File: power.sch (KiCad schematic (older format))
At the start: 33 parts, among them U3 M3406, U4 XC6206P25, U5 XC6206P12, U6 ME2108A33M3, U7 ME2108A50M3

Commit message: Proto 1
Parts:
- added SW9: SW_SPDT_shielded, lib:Korean_Hroparts_K3_1296S, symbol spdt_sh:SW_SPDT_shielded
- L1: value 2u2 -> SWPA252010S4R7MT; footprint Inductor_SMD:L_1206_3216Metric_Pad1.42x1.75mm_HandSolder -> lib:SWPA25xx
- L2: renamed from L3; value 47u -> SWPA6045S470MT; footprint Inductor_SMD:L_1206_3216Metric_Pad1.42x1.75mm_HandSolder -> lib:SWPA60xx
- L3: renamed from L2; value 47u -> SWPA6045S470MT; footprint Inductor_SMD:L_1206_3216Metric_Pad1.42x1.75mm_HandSolder -> lib:SWPA60xx
- renumbered C27 to C21, C1 to C22, C28 to C23, C29 to C24, C30 to C25, C48 to C26, C49 to C27, C50 to C28, C31 to C29, C32 to C30, C33 to C31, C34 to C32, C35 to C33, D4 to D1, D1 to D2, R28 to R17, R11 to R18, R12 to R19, R29 to R20, R32 to R21, R13 to R22, R30 to R23, R31 to R24, U3 to U5, U4 to U6, U5 to U8, U6 to U9
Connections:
- net labels added: VBAT_ALWON
- wire segments 70 -> 72
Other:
- note added: "L2: 1-4.7uH, 50-150mR\n(is 4.7uH, 0.479mR)"
- note removed: "L2: 1-4.7uH, 50-150mR"

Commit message: WiP for proto 2
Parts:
- removed C27, C28: 10u, Capacitor_SMD:C_0805_2012Metric, symbol Device:C_Small
- removed C29, C30: 1u, Capacitor_SMD:C_0603_1608Metric, symbol Device:C_Small
- removed U7: ME2108A50M3, Package_TO_SOT_SMD:SOT-23, symbol ME2108A:ME2108A50M3
- removed U8: XC6206P12, Package_TO_SOT_SMD:SOT-23, symbol xc6206:XC6206P12
- removed U9: ME2108A33M3, Package_TO_SOT_SMD:SOT-23, symbol ME2108A:ME2108A33M3
- added C10, C11: 10u, Capacitor_SMD:C_0805_2012Metric, symbol Device:C_Small
- added C4: 22p, Capacitor_SMD:C_0805_2012Metric, symbol Device:C_Small
- added R24: 100K, Resistor_SMD:R_0603_1608Metric, symbol Device:R
- added R6: 330K, Resistor_SMD:R_0603_1608Metric, symbol Device:R
- added U7, U9: XR1151, Package_TO_SOT_SMD:SOT-23-6, symbol XR1151:XR1151
- D1, D2: value SS12 -> MBRA210LT3
- L2, L3: value SWPA6045S470MT -> LQH3NPN2R2MJRL; footprint lib:SWPA60xx -> Inductor_SMD:L_Murata_DEM35xxC
- R21: value 0 -> 82K
- R22: value NS -> 0
- R23: value 0 -> 560K
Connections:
- wire segments 72 -> 78
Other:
- note added: "1V1: 500mA max"
- note added: "5V: 500mA max"
- note added: "Note: M3406 and XR1151 are Chinesium,\nbut very cheap."
- note added: "VIO: 700mA max\n"
- note removed: "1V1 output: 500mA max"
- note removed: "1V1_serdes (if LDO): 200mA max"
- note removed: "5V: 200-300mA"
- note removed: "For 1V1_serdes, either stuff 0 ohm resistor or LDO logic.\nNeither are needed for the -U FPGA instead of the -UM one.\nNote that the LDO *should* be 1V1, but we cheat a bit. (Makes \nit work up to 5G, though.)"
- note removed: "L2: >=600mA"
- note removed: "Note: M3406 is Chinesium,\nbut very cheap."
- note removed: "Output caps: >=16V"
- note removed: "VIO: 200-300mA"
- moved on the sheet: C24, C25, C31, C32, C33, D2, L3, R20, R24, U6

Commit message: Nearly done...
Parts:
- added C27: 22p, Capacitor_SMD:C_0603_1608Metric, symbol Device:C_Small
- C4: footprint Capacitor_SMD:C_0805_2012Metric -> Capacitor_SMD:C_0603_1608Metric
- L1: value SWPA252010S4R7MT -> LQH3NPN2R2MJRL; footprint lib:SWPA25xx -> lib:Murata_1212
- L2, L3: footprint Inductor_SMD:L_Murata_DEM35xxC -> lib:Murata_1212
- renumbered R24 to R47
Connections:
- net at C10.1, C11.1, D1.1 (K)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: now also C27.1
- net at R23.2, R47.1, U9.3 (FB): now also C27.2
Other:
- note added: "2V5: 200mA max\n(Note it draws from VIO)"
- note removed: "2V5 output: 200mA max\n(Note it also loads VIO)"
- moved on the sheet: C10, C11, R22
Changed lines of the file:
@@
 P 3550 1800
 F 0 "L1" V 3372 1800 50  0000 C CNN
-F 1 "SWPA252010S4R7MT" V 3250 1800 50  0000 C CNN
-F 2 "lib:SWPA25xx" H 3550 1800 50  0001 C CNN
+F 1 "LQH3NPN2R2MJRL" V 3250 1800 50  0000 C CNN
+F 2 "lib:Murata_1212" H 3550 1800 50  0001 C CNN
 F 3 "~" H 3550 1800 50  0001 C CNN
 	1    3550 1800
@@
 F 0 "L3" V 2472 4300 50  0000 C CNN
 F 1 "LQH3NPN2R2MJRL" V 2550 4050 50  0000 C CNN
-F 2 "Inductor_SMD:L_Murata_DEM35xxC" H 2650 4300 50  0001 C CNN
+F 2 "lib:Murata_1212" H 2650 4300 50  0001 C CNN
 F 3 "~" H 2650 4300 50  0001 C CNN
 	1    2650 4300
@@
 1V1: 500mA max
 Text Notes 3900 3450 0    50   ~ 0
-2V5 output: 200mA max\n(Note it also loads VIO)
+2V5: 200mA max\n(Note it draws from VIO)
 $Comp
 L Device:R R17
@@
 Text GLabel 2050 6300 0    50   Input ~ 0
 VBAT
-Text GLabel 4900 5950 2    50   Input ~ 0
+Text GLabel 5150 5950 2    50   Input ~ 0
 5V
 $Comp
@@
 F 0 "L2" V 2472 5950 50  0000 C CNN
 F 1 "LQH3NPN2R2MJRL" V 2550 5700 50  0000 C CNN
-F 2 "Inductor_SMD:L_Murata_DEM35xxC" H 2650 5950 50  0001 C CNN
+F 2 "lib:Murata_1212" H 2650 5950 50  0001 C CNN
 F 3 "~" H 2650 5950 50  0001 C CNN
 	1    2650 5950
@@
 L Device:C_Small C10
 U 1 1 5D06339F
-P 4000 6200
-F 0 "C10" H 4092 6246 50  0000 L CNN
-F 1 "10u" H 4092 6155 50  0000 L CNN
-F 2 "Capacitor_SMD:C_0805_2012Metric" H 4000 6200 50  0001 C CNN
-F 3 "~" H 4000 6200 50  0001 C CNN
-	1    4000 6200
+P 4250 6200
+F 0 "C10" H 4342 6246 50  0000 L CNN
+F 1 "10u" H 4342 6155 50  0000 L CNN
+F 2 "Capacitor_SMD:C_0805_2012Metric" H 4250 6200 50  0001 C CNN
+F 3 "~" H 4250 6200 50  0001 C CNN
+	1    4250 6200
 	1    0    0    -1
 $EndComp
@@
 L Device:C_Small C11
 U 1 1 5D0633A5
-P 4350 6200
-F 0 "C11" H 4442 6246 50  0000 L CNN
-F 1 "10u" H 4442 6155 50  0000 L CNN
-F 2 "Capacitor_SMD:C_0805_2012Metric" H 4350 6200 50  0001 C CNN
-F 3 "~" H 4350 6200 50  0001 C CNN
-	1    4350 6200
+P 4600 6200
+F 0 "C11" H 4692 6246 50  0000 L CNN
+F 1 "10u" H 4692 6155 50  0000 L CNN
+F 2 "Capacitor_SMD:C_0805_2012Metric" H 4600 6200 50  0001 C CNN
+F 3 "~" H 4600 6200 50  0001 C CNN
+	1    4600 6200
 	1    0    0    -1
 $EndComp
@@
 L power:GND #PWR0105
 U 1 1 5D0633B7
-P 4000 6450
-F 0 "#PWR0105" H 4000 6200 50  0001 C CNN
-F 1 "GND" H 4005 6277 50  0000 C CNN
-F 2 "" H 4000 6450 50  0001 C CNN
-F 3 "" H 4000 6450 50  0001 C CNN
-	1    4000 6450
+P 4250 6450
+F 0 "#PWR0105" H 4250 6200 50  0001 C CNN
+F 1 "GND" H 4255 6277 50  0000 C CNN
+F 2 "" H 4250 6450 50  0001 C CNN
+F 3 "" H 4250 6450 50  0001 C CNN
+	1    4250 6450
 	1    0    0    -1
 $EndComp
@@
 L Device:R R22
 U 1 1 5D0633C9
-P 4650 5950
-F 0 "R22" V 4443 5950 50  0000 C CNN
-F 1 "0" V 4534 5950 50  0000 C CNN
-F 2 "Resistor_SMD:R_0603_1608Metric" V 4580 5950 50  0001 C CNN
-F 3 "~" H 4650 5950 50  0001 C CNN
-	1    4650 5950
+P 4900 5950
+F 0 "R22" V 4693 5950 50  0000 C CNN
+F 1 "0" V 4784 5950 50  0000 C CNN
+F 2 "Resistor_SMD:R_0603_1608Metric" V 4830 5950 50  0001 C CNN
+F 3 "~" H 4900 5950 50  0001 C CNN
+	1    4900 5950
 	0    1    1    0
 $EndComp
@@
 $EndComp
 $Comp
-L Device:R R24
+L Device:R R47
 U 1 1 5D0633DB
 P 3650 6800
-F 0 "R24" H 3720 6846 50  0000 L CNN
+F 0 "R47" H 3720 6846 50  0000 L CNN
 F 1 "100K" H 3720 6755 50  0000 L CNN
 F 2 "Resistor_SMD:R_0603_1608Metric" V 3580 6800 50  0001 C CNN
@@
 	3650 5950 3650 6100
 Wire Wire Line
-	3650 5950 4000 5950
-Connection ~ 3650 5950
-Wire Wire Line
-	4350 6100 4350 5950
-Connection ~ 4350 5950
-Wire Wire Line
-	4350 5950 4500 5950
-Wire Wire Line
-	4000 6100 4000 5950
-Connection ~ 4000 5950
-Wire Wire Line
-	4000 5950 4350 5950
+	3900 5950 4250 5950
+Wire Wire Line
+	4600 6100 4600 5950
+Connection ~ 4600 5950
+Wire Wire Line
+	4600 5950 4750 5950
+Wire Wire Line
+	4250 6100 4250 5950
+Connection ~ 4250 5950
+Wire Wire Line
+	4250 5950 4600 5950
 Wire Wire Line
 	3500 6550 3650 6550
@@
 Connection ~ 3650 6550
 Wire Wire Line
-	4000 6450 4000 6300
+	4250 6450 4250 6300
 $Comp
 L power:GND #PWR0107
 U 1 1 5D0633FE
-P 4350 6450
-F 0 "#PWR0107" H 4350 6200 50  0001 C CNN
-F 1 "GND" H 4355 6277 50  0000 C CNN
-F 2 "" H 4350 6450 50  0001 C CNN
-F 3 "" H 4350 6450 50  0001 C CNN
-	1    4350 6450
-	1    0    0    -1
-$EndComp
-Wire Wire Line
-	4350 6300 4350 6450
-Wire Wire Line
-	4800 5950 4900 5950
-Text Notes 4650 6150 0    50   ~ 0
+P 4600 6450
+F 0 "#PWR0107" H 4600 6200 50  0001 C CNN
+F 1 "GND" H 4605 6277 50  0000 C CNN
+F 2 "" H 4600 6450 50  0001 C CNN
+F 3 "" H 4600 6450 50  0001 C CNN
+	1    4600 6450
+	1    0    0    -1
+$EndComp
+Wire Wire Line
+	4600 6300 4600 6450
+Wire Wire Line
+	5050 5950 5150 5950
+Text Notes 4900 6150 0    50   ~ 0
 5V: 500mA max
 $Comp
@@
 F 0 "C4" H 3992 4646 50  0000 L CNN
 F 1 "22p" H 3992 4555 50  0000 L CNN
-F 2 "Capacitor_SMD:C_0805_2012Metric" H 3900 4600 50  0001 C CNN
+F 2 "Capacitor_SMD:C_0603_1608Metric" H 3900 4600 50  0001 C CNN
 F 3 "~" H 3900 4600 50  0001 C CNN
 	1    3900 4600
 	1    0    0    -1
 $EndComp
-Text Notes 4450 4350 0    50   ~ 0
-VIO: 700mA max\n
 Wire Wire Line
 	3650 4300 3900 4300
@@
 Wire Wire Line
 	3900 4900 3650 4900
+$Comp
+L Device:C_Small C27
+U 1 1 5D30B15A
+P 3900 6200
+F 0 "C27" H 3992 6246 50  0000 L CNN
+F 1 "22p" H 3992 6155 50  0000 L CNN
+F 2 "Capacitor_SMD:C_0603_1608Metric" H 3900 6200 50  0001 C CNN
+F 3 "~" H 3900 6200 50  0001 C CNN
+	1    3900 6200
+	1    0    0    -1
+$EndComp
+Wire Wire Line
+	3900 6100 3900 5950
+Wire Wire Line
+	3650 5950 3900 5950
+Connection ~ 3650 5950
+Connection ~ 3900 5950
+Wire Wire Line
+	3900 6550 3650 6550
+Wire Wire Line
+	3900 6300 3900 6550
 $EndSCHEMATC

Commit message: Proto2, final version
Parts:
- added C48: 100n, Capacitor_SMD:C_0603_1608Metric, symbol Device:C_Small
- added R58, R59: 100K, Resistor_SMD:R_0603_1608Metric, symbol Device:R
- BT1, BT2: Notes (none) -> https://item.taobao.com/item.htm?spm=a1z09.2.0.0.67002e8d5S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
- SW9: Notes (none) -> https://lcsc.com/product-detail/Toggle-Switches_Korean-Hrop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
- U5: Notes (none) -> Xian Aerosemi Tech M3406-ADJ
- U6: Notes (none) -> Torex XC6206P252MR
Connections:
- net GND: now also C48.2, R59.2
- net VBAT: now also R58.1
- new net ADC1: C48.1, R58.2, R59.1
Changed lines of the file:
@@
 F 2 "Package_TO_SOT_SMD:SOT-23-5" H 2900 2000 50  0001 C CNN
 F 3 "" H 2900 2000 50  0001 C CNN
+F 4 "Xian Aerosemi Tech M3406-ADJ" H 2900 2000 50  0001 C CNN "Notes"
 	1    2900 2000
 	1    0    0    -1
@@
 F 2 "lib:battery_holder_1xAA" V 1250 2260 50  0001 C CNN
 F 3 "~" V 1250 2260 50  0001 C CNN
+F 4 "https://item.taobao.com/item.htm?spm=a1z09.2.0.0.67002e8d5Si8Ic&id=543590913112&_u=h2c9d2uc565f" H 1250 2200 50  0001 C CNN "Notes"
 	1    1250 2200
 	1    0    0    -1
@@
 F 2 "lib:battery_holder_1xAA" V 1250 2560 50  0001 C CNN
 F 3 "~" V 1250 2560 50  0001 C CNN
+F 4 "https://item.taobao.com/item.htm?spm=a1z09.2.0.0.67002e8d5Si8Ic&id=543590913112&_u=h2c9d2uc565f" H 1250 2500 50  0001 C CNN "Notes"
 	1    1250 2500
 	1    0    0    -1
@@
 F 2 "Package_TO_SOT_SMD:SOT-23" H 2900 3250 50  0001 C CNN
 F 3 "" H 2900 3250 50  0001 C CNN
+F 4 "Torex XC6206P252MR" H 2900 3250 50  0001 C CNN "Notes"
 	1    2900 3250
 	1    0    0    -1
@@
 F 2 "lib:Korean_Hroparts_K3_1296S" H 6700 1950 50  0001 C CNN
 F 3 "" H 6700 1950 50  0001 C CNN
+F 4 "https://lcsc.com/product-detail/Toggle-Switches_Korean-Hroparts-Elec-K3-1296S-E1_C128955.html" H 6700 1950 50  0001 C CNN "Notes"
 	1    6700 1950
 	1    0    0    -1
@@
 Wire Wire Line
 	3900 6300 3900 6550
+Text GLabel 6450 3250 0    50   Input ~ 0
+ADC1
+Text GLabel 6450 2850 0    50   Input ~ 0
+VBAT
+$Comp
+L Device:R R58
+U 1 1 5D3BD728
+P 6600 3050
+F 0 "R58" H 6670 3096 50  0000 L CNN
+F 1 "100K" H 6670 3005 50  0000 L CNN
+F 2 "Resistor_SMD:R_0603_1608Metric" V 6530 3050 50  0001 C CNN
+F 3 "~" H 6600 3050 50  0001 C CNN
+	1    6600 3050
+	1    0    0    -1
+$EndComp
+$Comp
+L Device:R R59
+U 1 1 5D3BDE34
+P 6600 3500
+F 0 "R59" H 6670 3546 50  0000 L CNN
+F 1 "100K" H 6670 3455 50  0000 L CNN
+F 2 "Resistor_SMD:R_0603_1608Metric" V 6530 3500 50  0001 C CNN
+F 3 "~" H 6600 3500 50  0001 C CNN
+	1    6600 3500
+	1    0    0    -1
+$EndComp
+$Comp
+L power:GND #PWR0117
+U 1 1 5D3BE494
+P 6600 3800
+F 0 "#PWR0117" H 6600 3550 50  0001 C CNN
+F 1 "GND" H 6605 3627 50  0000 C CNN
+F 2 "" H 6600 3800 50  0001 C CNN
+F 3 "" H 6600 3800 50  0001 C CNN
+	1    6600 3800
+	1    0    0    -1
+$EndComp
+Wire Wire Line
+	6450 3250 6600 3250
+Wire Wire Line
+	6600 3250 6600 3200
+Wire Wire Line
+	6600 3250 6600 3350
+Connection ~ 6600 3250
+Wire Wire Line
+	6600 3650 6600 3800
+Wire Wire Line
+	6600 2900 6600 2850
+Wire Wire Line
+	6600 2850 6450 2850
+$Comp
+L Device:C_Small C48
+U 1 1 5D3CDC6D
+P 7000 3500
+F 0 "C48" H 7092 3546 50  0000 L CNN
+F 1 "100n" H 7092 3455 50  0000 L CNN
+F 2 "Capacitor_SMD:C_0603_1608Metric" H 7000 3500 50  0001 C CNN
+F 3 "~" H 7000 3500 50  0001 C CNN
+	1    7000 3500
+	1    0    0    -1
+$EndComp
+$Comp
+L power:GND #PWR0123
+U 1 1 5D3CF35A
+P 7000 3800
+F 0 "#PWR0123" H 7000 3550 50  0001 C CNN
+F 1 "GND" H 7005 3627 50  0000 C CNN
+F 2 "" H 7000 3800 50  0001 C CNN
+F 3 "" H 7000 3800 50  0001 C CNN
+	1    7000 3800
+	1    0    0    -1
+$EndComp
+Wire Wire Line
+	7000 3600 7000 3800
+Wire Wire Line
+	7000 3400 7000 3250
+Wire Wire Line
+	7000 3250 6600 3250
 $EndSCHEMATC

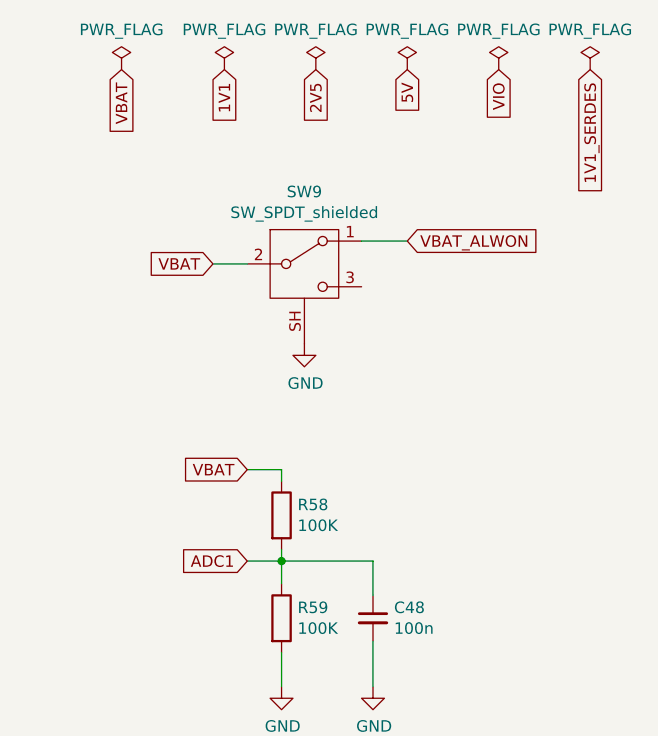
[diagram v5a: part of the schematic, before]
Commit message: Fix fab drawings to make sense
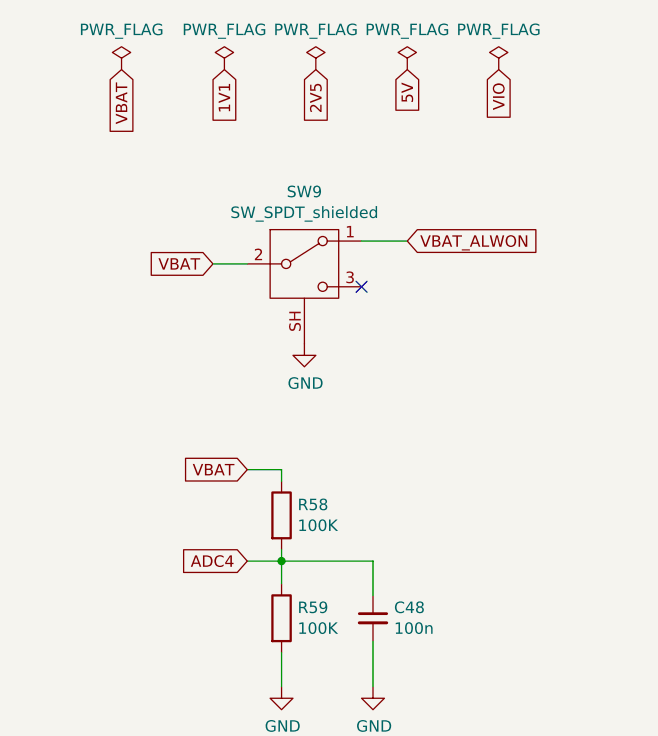
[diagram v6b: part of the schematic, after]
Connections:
- net ADC1 renamed ADC4
- no-connect marks 0 -> 1
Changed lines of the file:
@@
 VIO
-$Comp
-L power:PWR_FLAG #FLG0106
-U 1 1 5C9E1310
-P 7950 1100
-F 0 "#FLG0106" H 7950 1175 50  0001 C CNN
-F 1 "PWR_FLAG" H 7950 1274 50  0000 C CNN
-F 2 "" H 7950 1100 50  0001 C CNN
-F 3 "~" H 7950 1100 50  0001 C CNN
-	1    7950 1100
-	1    0    0    -1
-$EndComp
-Text GLabel 7950 1100 3    50   Input ~ 0
-1V1_SERDES
 $Comp
 L power:PWR_FLAG #FLG0108
@@
 	3900 6300 3900 6550
 Text GLabel 6450 3250 0    50   Input ~ 0
-ADC1
+ADC4
 Text GLabel 6450 2850 0    50   Input ~ 0
 VBAT
@@
 Wire Wire Line
 	7000 3250 6600 3250
+NoConn ~ 6950 2050
 $EndSCHEMATC

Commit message: This is proto 3.
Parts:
- added A1: art, lib:badge_art, symbol art:art
- added Q2: AO3401, Package_TO_SOT_SMD:SOT-23, symbol jeroens_components:AO3401
- R23: value 560K -> 750K
- R6: value 330K -> 360K
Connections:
- net GND: now also Q2.1 (G)
- net VBAT_ALWON: now also Q2.2 (S); no longer BT1.1 (+)
- new net: BT1.1 (+), Q2.3 (D)
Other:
- note added: "Battery voltage\nmeasurement"
- note added: "Note: M3406 and XR1151 are Chinesium,\nbut very cheap and plenty good."
- note added: "Reverse polarity\nprotection"
- note added: "VIO: 3.3V \n@ 700mA max\n"
- note removed: "Note: M3406 and XR1151 are Chinesium,\nbut very cheap."
- note removed: "VIO: 700mA max\n"
- moved on the sheet: BT1, BT2
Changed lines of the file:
@@
 EESchema Schematic File Version 4
 LIBS:hadbadge2019-cache
-EELAYER 29 0
+EELAYER 30 0
 EELAYER END
 $Descr A4 11693 8268
@@
 	1    0    0    -1
 $EndComp
-$Comp
-L Device:Battery_Cell BT1
-U 1 1 5C5EF231
-P 1250 2200
-F 0 "BT1" H 1368 2296 50  0000 L CNN
-F 1 "Battery_Cell" H 1368 2205 50  0000 L CNN
-F 2 "lib:battery_holder_1xAA" V 1250 2260 50  0001 C CNN
-F 3 "~" V 1250 2260 50  0001 C CNN
-F 4 "https://item.taobao.com/item.htm?spm=a1z09.2.0.0.67002e8d5Si8Ic&id=543590913112&_u=h2c9d2uc565f" H 1250 2200 50  0001 C CNN "Notes"
-	1    1250 2200
-	1    0    0    -1
-$EndComp
-$Comp
-L Device:Battery_Cell BT2
-U 1 1 5C5EF2C3
-P 1250 2500
-F 0 "BT2" H 1368 2596 50  0000 L CNN
-F 1 "Battery_Cell" H 1368 2505 50  0000 L CNN
-F 2 "lib:battery_holder_1xAA" V 1250 2560 50  0001 C CNN
-F 3 "~" V 1250 2560 50  0001 C CNN
-F 4 "https://item.taobao.com/item.htm?spm=a1z09.2.0.0.67002e8d5Si8Ic&id=543590913112&_u=h2c9d2uc565f" H 1250 2500 50  0001 C CNN "Notes"
-	1    1250 2500
-	1    0    0    -1
-$EndComp
 Text GLabel 1250 1850 1    50   Input ~ 0
 VBAT_ALWON
-Wire Wire Line
-	1250 1850 1250 2000
 $Comp
 L power:GND #PWR033
 U 1 1 5C5EF389
-P 1250 2600
-F 0 "#PWR033" H 1250 2350 50  0001 C CNN
-F 1 "GND" H 1255 2427 50  0000 C CNN
-F 2 "" H 1250 2600 50  0001 C CNN
-F 3 "" H 1250 2600 50  0001 C CNN
-	1    1250 2600
+P 1250 3000
+F 0 "#PWR033" H 1250 2750 50  0001 C CNN
+F 1 "GND" H 1255 2827 50  0000 C CNN
+F 2 "" H 1250 3000 50  0001 C CNN
+F 3 "" H 1250 3000 50  0001 C CNN
+	1    1250 3000
 	1    0    0    -1
 $EndComp
@@
 LDO dropout voltage is 0.3-0.7V... so we need 2.8-3.2V of \ninput. Not enough margin with just 2 AA cells: If any, NiMHs\nwill break this (2.4V max). Hence, we need a SMPS to generate\n the 3.3VIO, and from that derive the 2.5V Vaux.
 Text Notes 3300 1200 0    50   ~ 0
-Note: M3406 and XR1151 are Chinesium,\nbut very cheap.
+Note: M3406 and XR1151 are Chinesium,\nbut very cheap and plenty good.
 Text GLabel 2050 4650 0    50   Input ~ 0
 VBAT
@@
 P 3650 4600
 F 0 "R6" H 3720 4646 50  0000 L CNN
-F 1 "330K" H 3720 4555 50  0000 L CNN
+F 1 "360K" H 3720 4555 50  0000 L CNN
 F 2 "Resistor_SMD:R_0603_1608Metric" V 3580 4600 50  0001 C CNN
 F 3 "~" H 3650 4600 50  0001 C CNN
@@
 Wire Wire Line
 	5050 4300 5150 4300
-Text Notes 4900 4500 0    50   ~ 0
-VIO: 700mA max\n
+Text Notes 4900 4550 0    50   ~ 0
+VIO: 3.3V \n@ 700mA max\n
 Text GLabel 2050 6300 0    50   Input ~ 0
 VBAT
@@
 P 3650 6250
 F 0 "R23" H 3720 6296 50  0000 L CNN
-F 1 "560K" H 3720 6205 50  0000 L CNN
+F 1 "750K" H 3720 6205 50  0000 L CNN
 F 2 "Resistor_SMD:R_0603_1608Metric" V 3580 6250 50  0001 C CNN
 F 3 "~" H 3650 6250 50  0001 C CNN
@@
 	7000 3250 6600 3250
 NoConn ~ 6950 2050
+Text Notes 550  2050 0    50   ~ 0
+Reverse polarity\nprotection
+Text Notes 6900 3000 0    50   ~ 0
+Battery voltage\nmeasurement
+$Comp
+L Device:Battery_Cell BT2
+U 1 1 5C5EF2C3
+P 1250 2900
+F 0 "BT2" H 1368 2996 50  0000 L CNN
+F 1 "Battery_Cell" H 1368 2905 50  0000 L CNN
+F 2 "lib:battery_holder_1xAA" V 1250 2960 50  0001 C CNN
+F 3 "~" V 1250 2960 50  0001 C CNN
+F 4 "https://item.taobao.com/item.htm?spm=a1z09.2.0.0.67002e8d5Si8Ic&id=543590913112&_u=h2c9d2uc565f" H 1250 2900 50  0001 C CNN "Notes"
+	1    1250 2900
+	1    0    0    -1
+$EndComp
+$Comp
+L Device:Battery_Cell BT1
+U 1 1 5C5EF231
+P 1250 2600
+F 0 "BT1" H 1368 2696 50  0000 L CNN
+F 1 "Battery_Cell" H 1368 2605 50  0000 L CNN
+F 2 "lib:battery_holder_1xAA" V 1250 2660 50  0001 C CNN
+F 3 "~" V 1250 2660 50  0001 C CNN
+F 4 "https://item.taobao.com/item.htm?spm=a1z09.2.0.0.67002e8d5Si8Ic&id=543590913112&_u=h2c9d2uc565f" H 1250 2600 50  0001 C CNN "Notes"
+	1    1250 2600
+	1    0    0    -1
+$EndComp
+$Comp
+L jeroens_components:AO3401 Q2
+U 1 1 5D6A27A7
+P 1350 2200
+F 0 "Q2" H 1556 2154 50  0000 L CNN
+F 1 "AO3401" H 1556 2245 50  0000 L CNN
+F 2 "Package_TO_SOT_SMD:SOT-23" H 1550 2125 50  0001 L CIN
+F 3 "http://www.aosmd.com/res/data_sheets/AO3401.pdf" H 1350 2200 50  0001 L CNN
+	1    1350 2200
+	-1   0    0    1
+$EndComp
+$Comp
+L power:GND #PWR0126
+U 1 1 5D6A7E95
+P 1700 2300
+F 0 "#PWR0126" H 1700 2050 50  0001 C CNN
+F 1 "GND" H 1705 2127 50  0000 C CNN
+F 2 "" H 1700 2300 50  0001 C CNN
+F 3 "" H 1700 2300 50  0001 C CNN
+	1    1700 2300
+	1    0    0    -1
+$EndComp
+Wire Wire Line
+	1550 2200 1700 2200
+Wire Wire Line
+	1700 2200 1700 2300
+Wire Wire Line
+	1250 1850 1250 2000
+$Comp
+L art:art A1
+U 1 1 5D6694BE
+P 7450 5200
+F 0 "A1" H 7778 5296 50  0000 L CNN
+F 1 "art" H 7778 5205 50  0000 L CNN
+F 2 "lib:badge_art" H 7450 5550 50  0001 C CNN
+F 3 "" H 7450 5550 50  0001 C CNN
+	1    7450 5200
+	1    0    0    -1
+$EndComp
 $EndSCHEMATC

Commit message: Starting to add fixes for final ver
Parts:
- added H1: MountingHole, MountingHole:MountingHole_3.5mm, symbol Mechanical:MountingHole
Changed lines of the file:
@@
+	1    0    0    -1
+$EndComp
+$Comp
+L Mechanical:MountingHole H1
+U 1 1 5DBAD1B3
+P 6350 5100
+F 0 "H1" H 6450 5146 50  0000 L CNN
+F 1 "MountingHole" H 6450 5055 50  0000 L CNN
+F 2 "MountingHole:MountingHole_3.5mm" H 6350 5100 50  0001 C CNN
+F 3 "~" H 6350 5100 50  0001 C CNN
+	1    6350 5100
 	1    0    0    -1
 $EndComp
